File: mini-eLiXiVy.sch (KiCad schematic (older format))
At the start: 175 parts, among them J1 TYPE-C-31-M12_13_EDITED, J2 AVR-ISP-6, SW1 SW_Push, U1 ATmega32U4-AU, U2 WE-TVS-82400102, Y1 Crystal_GND24_Small

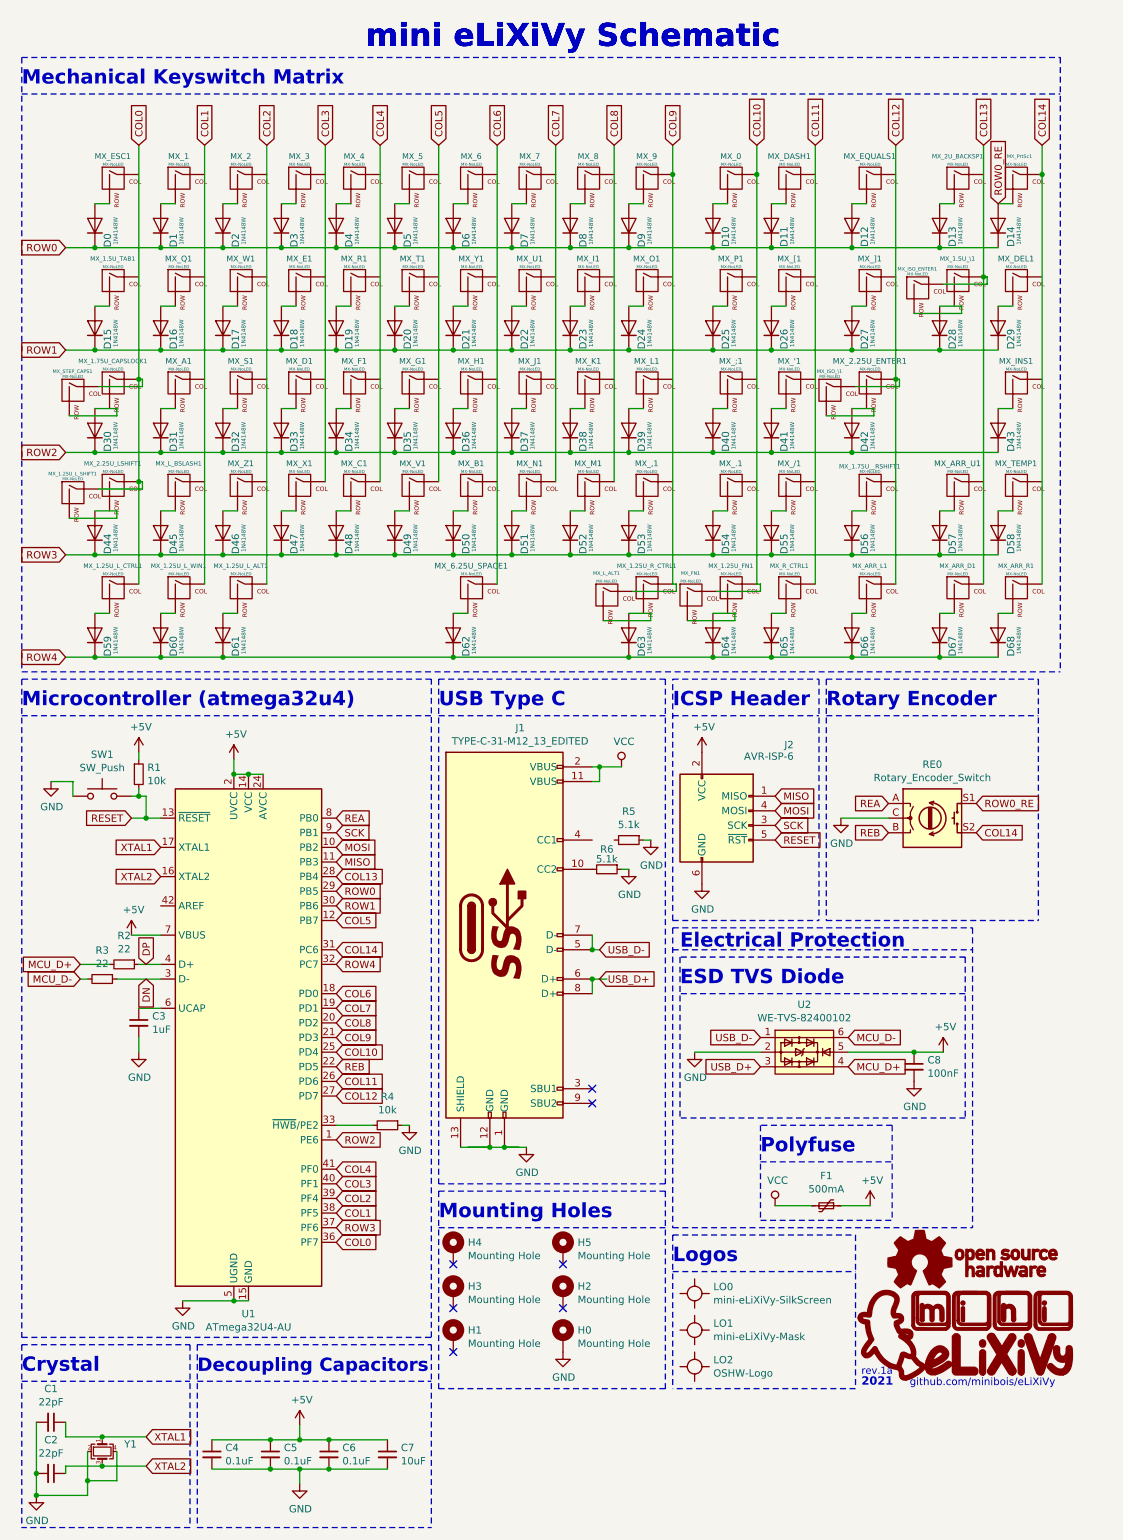
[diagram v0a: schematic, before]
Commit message: Reconnected some of the traces
After changing library locations around, some switches were disconnected in the schematic.
Had to reconnect those.
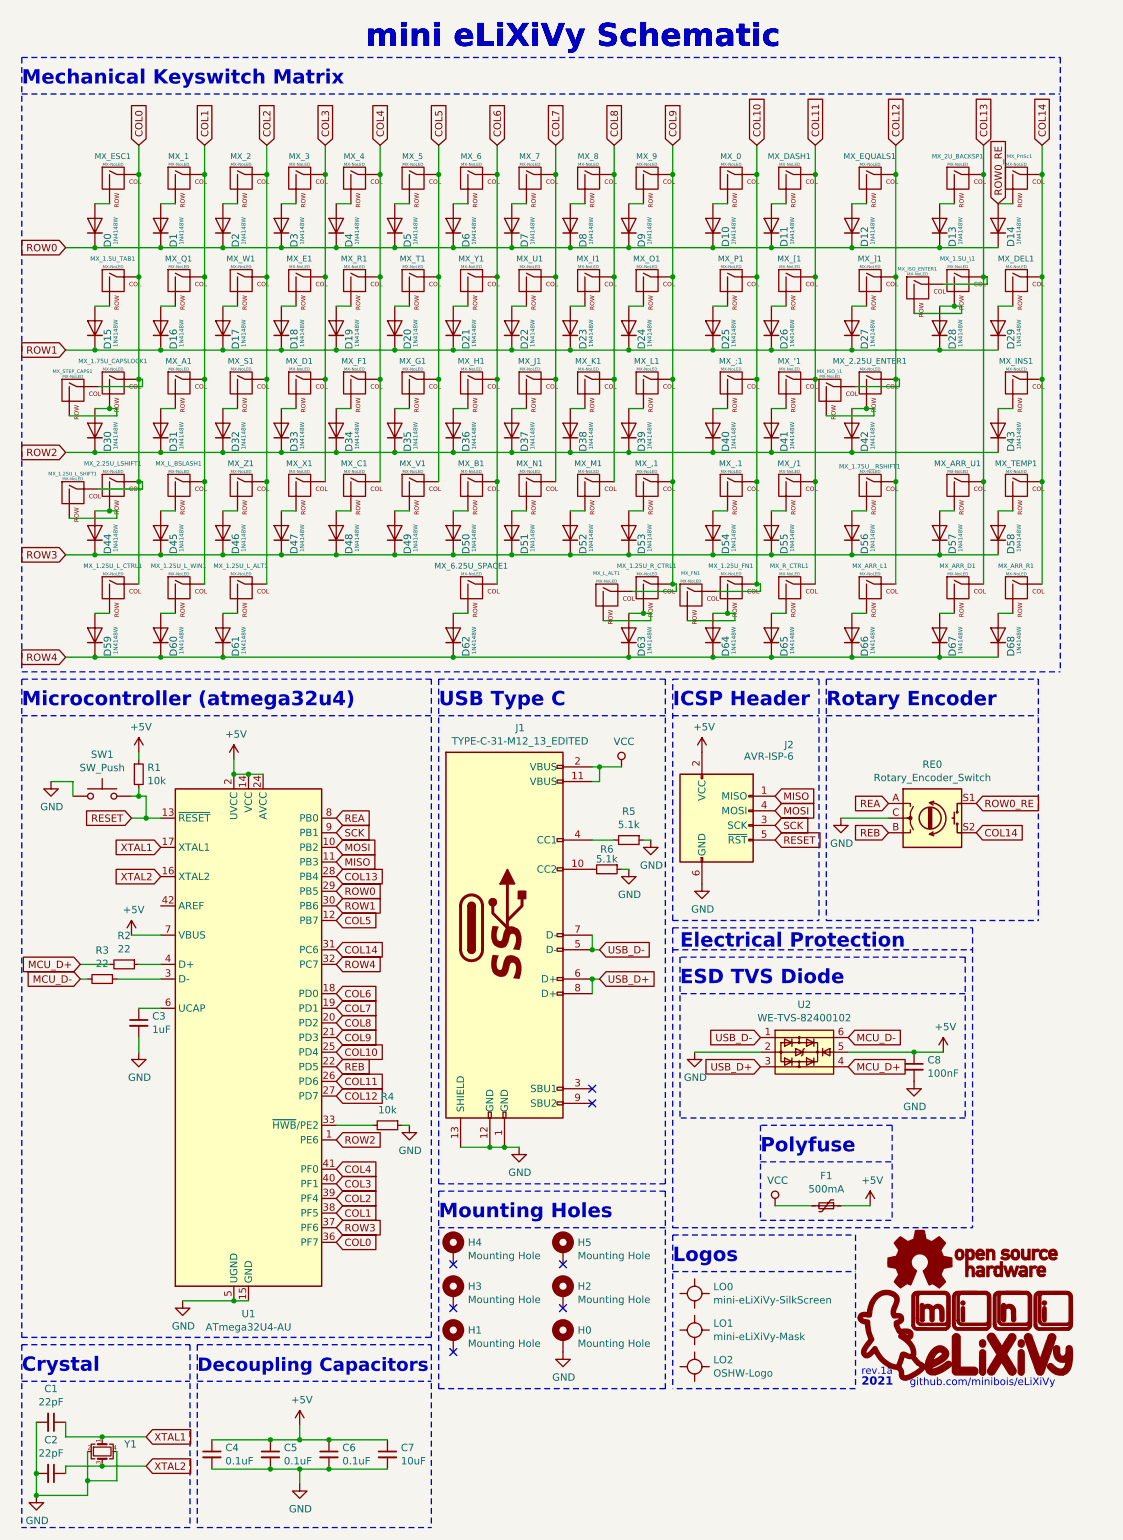
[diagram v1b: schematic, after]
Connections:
- net COL0: now also MX_1.5U_TAB1.1 (COL), MX_ESC1.1 (COL)
- net COL1: now also MX_1.1 (COL), MX_A1.1 (COL), MX_L_BSLASH1.1 (COL), MX_Q1.1 (COL)
- net COL10: now also MX_.1.1 (COL), MX_;1.1 (COL), MX_P1.1 (COL)
- net COL11: now also MX_'1.1 (COL), MX_/1.1 (COL), MX_DASH1.1 (COL), MX_[1.1 (COL)
- net COL12: now also MX_1.75U__RSHIFT1.1 (COL), MX_EQUALS1.1 (COL), MX_]1.1 (COL)
- net COL13: now also MX_2U_BACKSP1.1 (COL), MX_ARR_U1.1 (COL)
- net COL14: now also MX_DEL1.1 (COL), MX_INS1.1 (COL), MX_TEMP1.1 (COL)
- net COL2: now also MX_2.1 (COL), MX_S1.1 (COL), MX_W1.1 (COL), MX_Z1.1 (COL)
- net COL3: now also MX_3.1 (COL), MX_D1.1 (COL), MX_E1.1 (COL)
- net COL4: now also MX_4.1 (COL), MX_F1.1 (COL), MX_R1.1 (COL)
- net COL5: now also MX_5.1 (COL), MX_G1.1 (COL), MX_T1.1 (COL)
- net COL6: now also MX_6.1 (COL), MX_B1.1 (COL), MX_H1.1 (COL), MX_Y1.1 (COL)
- net COL7: now also MX_7.1 (COL), MX_J1.1 (COL), MX_U1.1 (COL)
- net COL8: now also MX_8.1 (COL), MX_I1.1 (COL), MX_K1.1 (COL)
- net COL9: now also MX_,1.1 (COL), MX_L1.1 (COL), MX_O1.1 (COL)
- net at MX_1.75U_CAPSLOCK1.2 (ROW): now also D30.2 (A), MX_STEP_CAPS1.2 (ROW)
- net at MX_2.25U_LSHIFT1.2 (ROW): now also D44.2 (A), MX_1.25U_L_SHIFT1.2 (ROW)
- net at MX_1.25U_R_CTRL1.2 (ROW): now also D63.2 (A), MX_L_ALT1.2 (ROW)
- net at MX_1.25U_FN1.2 (ROW): now also D64.2 (A), MX_FN1.2 (ROW)
- net at MX_2.25U_ENTER1.2 (ROW): now also D42.2 (A), MX_ISO_\1.2 (ROW)
- net at MX_1.5U_\1.2 (ROW): now also D28.2 (A), MX_ISO_ENTER1.2 (ROW)
- net at R5.2: now also J1.4 (CC1)
- net DN: no longer names the net of R3.1, U1.3 (D-)
- net DP: no longer names the net of R2.1, U1.4 (D+)
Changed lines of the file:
@@
 	6275 3500 7275 3500
 Wire Wire Line
-	6275 2800 6875 2800
-Wire Wire Line
 	6275 2100 6875 2100
-Wire Wire Line
-	6700 2550 7025 2550
 Wire Wire Line
 	6900 2350 7200 2350
@@
 Connection ~ 1550 3500
 Connection ~ 1975 3500
-Connection ~ 1100 3500
-Wire Wire Line
-	1100 3500 1550 3500
 Wire Wire Line
 	1550 4200 1975 4200
@@
 	1975 3500 2375 3500
 Wire Wire Line
-	900  3500 1100 3500
-Wire Wire Line
-	6875 2800 7275 2800
-Connection ~ 6875 2800
-Wire Wire Line
 	5325 2800 5725 2800
 Wire Wire Line
@@
 Wire Wire Line
 	900  2100 1100 2100
-Connection ~ 7175 2300
 Wire Wire Line
 	7200 2300 7200 2350
 Wire Wire Line
 	7175 2300 7200 2300
-Connection ~ 6575 3000
 Wire Wire Line
 	6600 3000 6600 3050
@@
 $EndComp
 $Comp
-L Diode:1N4148W D30
-U 1 1 622FC3F7
-P 1100 3350
-F 0 "D30" H 1095 3263 50  0000 R CNN
-F 1 "1N4148W" H 1159 3208 28  0000 R CNN
-F 2 "mini-general-tweaks:D_SOD123_axial-dual" H 1100 3175 50  0001 C CNN
-F 3 "https://www.vishay.com/docs/85748/1n4148w.pdf" H 1100 3350 50  0001 C CNN
-	1    1100 3350
-	0    -1   -1   0
-$EndComp
-$Comp
 L Diode:1N4148W D15
 U 1 1 622EF341
@@
 	1    0    0    -1
 $EndComp
-Wire Wire Line
-	7025 2500 7025 2550
 Wire Wire Line
 	5825 4600 5725 4600
@@
 Text Notes 2950 750  0    157  ~ 31
 mini eLiXiVy Schematic
-Connection ~ 5050 1600
-Wire Wire Line
-	5050 1600 5050 1400
-Connection ~ 5625 1600
 Wire Wire Line
 	5625 1600 5625 1400
-Connection ~ 7575 1600
 Wire Wire Line
 	7575 1600 7575 1400
@@
 Text Notes 3450 5250 0    98   ~ 20
 USB Type C
-Connection ~ 4500 7100
 Connection ~ 4500 6900
 Wire Wire Line
@@
 L power:GND #PWR0101
 U 1 1 607575CF
-P 4050 8250
-F 0 "#PWR0101" H 4050 8000 50  0001 C CNN
-F 1 "GND" H 4055 8077 50  0000 C CNN
-F 2 "" H 4050 8250 50  0001 C CNN
-F 3 "" H 4050 8250 50  0001 C CNN
-	1    4050 8250
-	1    0    0    -1
-$EndComp
-Wire Wire Line
-	3600 8250 3800 8250
-Connection ~ 3800 8250
-Wire Wire Line
-	3800 8250 3900 8250
-Connection ~ 3900 8250
-Wire Wire Line
-	3900 8250 4000 8250
+P 4000 8250
+F 0 "#PWR0101" H 4000 8000 50  0001 C CNN
+F 1 "GND" H 4005 8077 50  0000 C CNN
+F 2 "" H 4000 8250 50  0001 C CNN
+F 3 "" H 4000 8250 50  0001 C CNN
+	1    4000 8250
+	1    0    0    -1
+$EndComp
 $Comp
 L Device:R_Small R5
@@
 Text Notes 2950 750  0    157  ~ 31
 mini eLiXiVy Schematic
-Text GLabel 1450 7000 1    50   Input ~ 0
-DP
-Text GLabel 1450 7100 3    50   Input ~ 0
-DN
 Text Notes 6670 9892 0    51   ~ 0
 github.com/minibois/eLiXiVy
@@
 	5050 8800 7100 8800
 Wire Wire Line
-	7175 2300 7175 4400
-Wire Wire Line
-	7175 1400 7175 2300
-Wire Wire Line
-	6575 3000 6575 4400
-Wire Wire Line
-	6875 2500 7025 2500
-Wire Wire Line
-	4750 4600 4900 4600
-Wire Wire Line
-	6275 3200 6425 3200
-Wire Wire Line
-	1100 3200 1250 3200
-Wire Wire Line
-	1100 3900 1250 3900
-Wire Wire Line
-	5325 4600 5475 4600
-Wire Wire Line
-	3650 8250 3800 8250
-Wire Wire Line
-	5050 1600 5050 4400
-Wire Wire Line
-	5625 1600 5625 4400
-Wire Wire Line
-	7575 1600 7575 4400
-Wire Wire Line
-	3900 8250 4050 8250
-Wire Wire Line
-	1400 1400 1400 3000
-Wire Wire Line
-	1850 1400 1850 4400
-Wire Wire Line
-	2275 1400 2275 4400
-Wire Wire Line
-	2675 1400 2675 3700
-Wire Wire Line
-	3050 1400 3050 3700
-Wire Wire Line
-	3450 1400 3450 3700
-Wire Wire Line
-	3850 1400 3850 4400
-Wire Wire Line
-	4250 1400 4250 3700
-Wire Wire Line
-	4650 1400 4650 3700
-Wire Wire Line
-	6025 1400 6025 4400
-Wire Wire Line
-	6575 1400 6575 3000
-Wire Wire Line
-	4500 7100 4600 7100
+	6875 2500 6975 2500
 Wire Notes Line
 	7100 6750 7100 8800
@@
 Wire Wire Line
 	1400 5850 1450 5850
+Wire Wire Line
+	1100 3900 1200 3900
+Connection ~ 1200 3900
+Wire Wire Line
+	1200 3900 1250 3900
+Wire Wire Line
+	1850 4400 1850 3700
+Connection ~ 1850 1600
+Wire Wire Line
+	1850 1600 1850 1400
+Connection ~ 1850 2300
+Wire Wire Line
+	1850 2300 1850 1600
+Connection ~ 1850 3000
+Wire Wire Line
+	1850 3000 1850 2300
+Connection ~ 1850 3700
+Wire Wire Line
+	1850 3700 1850 3000
+Wire Wire Line
+	1400 1400 1400 1600
+Connection ~ 1400 1600
+Wire Wire Line
+	1400 1600 1400 2300
+Connection ~ 1400 2300
+Wire Wire Line
+	1400 2300 1400 3000
+Wire Wire Line
+	2275 1400 2275 1600
+Connection ~ 2275 1600
+Wire Wire Line
+	2275 1600 2275 2300
+Connection ~ 2275 2300
+Wire Wire Line
+	2275 2300 2275 3000
+Connection ~ 2275 3000
+Wire Wire Line
+	2275 3000 2275 3700
+Connection ~ 2275 3700
+Wire Wire Line
+	2275 3700 2275 4400
+Wire Wire Line
+	2675 1400 2675 1600
+Connection ~ 2675 1600
+Wire Wire Line
+	2675 1600 2675 2300
+Connection ~ 2675 2300
+Wire Wire Line
+	2675 2300 2675 3000
+Wire Wire Line
+	3050 1400 3050 1600
+Connection ~ 3050 1600
+Wire Wire Line
+	3050 1600 3050 2300
+Connection ~ 3050 2300
+Wire Wire Line
+	3050 2300 3050 3000
+Wire Wire Line
+	3450 1400 3450 1600
+Connection ~ 3450 1600
+Wire Wire Line
+	3450 1600 3450 2300
+Connection ~ 3450 2300
+Wire Wire Line
+	3450 2300 3450 3000
+Wire Wire Line
+	2675 3000 2675 3700
+Connection ~ 2675 3000
+Wire Wire Line
+	3050 3700 3050 3000
+Connection ~ 3050 3000
+Wire Wire Line
+	3450 3000 3450 3700
+Connection ~ 3450 3000
+Wire Wire Line
+	3850 3700 3850 3000
+Connection ~ 3850 1600
+Wire Wire Line
+	3850 1600 3850 1400
+Connection ~ 3850 2300
+Wire Wire Line
+	3850 2300 3850 1600
+Connection ~ 3850 3000
+Wire Wire Line
+	3850 3000 3850 2300
+Wire Wire Line
+	4250 1400 4250 1600
+Connection ~ 4250 1600
+Wire Wire Line
+	4250 1600 4250 2300
+Connection ~ 4250 2300
+Wire Wire Line
+	4250 2300 4250 3000
+Connection ~ 4250 3000
+Wire Wire Line
+	4250 3000 4250 3700
+Wire Wire Line
+	3850 4400 3850 3700
+Connection ~ 3850 3700
+Wire Wire Line
+	5050 4400 5050 3700
+Connection ~ 5050 4400
+Connection ~ 5050 1600
+Wire Wire Line
+	5050 1600 5050 1400
+Connection ~ 5050 2300
+Wire Wire Line
+	5050 2300 5050 1600
+Connection ~ 5050 3000
+Wire Wire Line
+	5050 3000 5050 2300
+Connection ~ 5050 3700
+Wire Wire Line
+	5050 3700 5050 3000
+Wire Wire Line
+	4650 1400 4650 1600
+Connection ~ 4650 1600
+Wire Wire Line
+	4650 1600 4650 2300
+Connection ~ 4650 2300
+Wire Wire Line
+	4650 2300 4650 3000
+Connection ~ 4650 3000
+Wire Wire Line
+	4650 3000 4650 3700
+Wire Wire Line
+	6025 4400 6025 3700
+Connection ~ 6025 1600
+Wire Wire Line
+	6025 1600 6025 1400
+Connection ~ 6025 2300
+Wire Wire Line
+	6025 2300 6025 1600
+Connection ~ 6025 3000
+Wire Wire Line
+	6025 3000 6025 2300
+Connection ~ 6025 3700
+Wire Wire Line
+	6025 3700 6025 3000
+Wire Wire Line
+	6575 1400 6575 1600
+Connection ~ 6575 1600
+Wire Wire Line
+	6575 1600 6575 2300
+Connection ~ 6575 2300
+Wire Wire Line
+	6575 2300 6575 3000
+Connection ~ 6575 3000
+Wire Wire Line
+	6575 3000 6575 3700
+Connection ~ 6575 3700
+Wire Wire Line
+	6575 3700 6575 4400
+Wire Wire Line
+	7175 4400 7175 3700
+Connection ~ 7175 1600
+Wire Wire Line
+	7175 1600 7175 1400
+Connection ~ 7175 2300
+Wire Wire Line
+	7175 2300 7175 1600
+Connection ~ 7175 3700
+Wire Wire Line
+	7175 3700 7175 2300
+Wire Wire Line
+	7575 1600 7575 2300
+Connection ~ 7575 1600
+Connection ~ 7575 2300
+Wire Wire Line
+	7575 2300 7575 3000
+Connection ~ 7575 3000
+Wire Wire Line
+	7575 3000 7575 3700
+Connection ~ 7575 3700
+Wire Wire Line
+	7575 3700 7575 4400
+Wire Wire Line
+	1100 3200 1200 3200
+Connection ~ 1200 3200
+Wire Wire Line
+	1200 3200 1250 3200
+Wire Wire Line
+	6275 2800 6875 2800
+Connection ~ 6875 2800
+Wire Wire Line
+	6875 2800 7275 2800
+Connection ~ 6975 2500
+Wire Wire Line
+	6975 2500 7025 2500
+Wire Wire Line
+	6700 2550 7025 2550
+Wire Wire Line
+	7025 2550 7025 2500
+Wire Wire Line
+	6275 3200 6375 3200
+Connection ~ 6375 3200
+Wire Wire Line
+	6375 3200 6425 3200
+Wire Wire Line
+	5625 4400 5625 3700
+Connection ~ 5625 4400
+Connection ~ 5625 1600
+Connection ~ 5625 2300
+Wire Wire Line
+	5625 2300 5625 1600
+Connection ~ 5625 3000
+Wire Wire Line
+	5625 3000 5625 2300
+Connection ~ 5625 3700
+Wire Wire Line
+	5625 3700 5625 3000
+Wire Wire Line
+	1100 3500 1550 3500
+Connection ~ 1100 3500
+Wire Wire Line
+	900  3500 1100 3500
+$Comp
+L Diode:1N4148W D30
+U 1 1 622FC3F7
+P 1100 3350
+F 0 "D30" H 1095 3263 50  0000 R CNN
+F 1 "1N4148W" H 1159 3208 28  0000 R CNN
+F 2 "mini-general-tweaks:D_SOD123_axial-dual" H 1100 3175 50  0001 C CNN
+F 3 "https://www.vishay.com/docs/85748/1n4148w.pdf" H 1100 3350 50  0001 C CNN
+	1    1100 3350
+	0    -1   -1   0
+$EndComp
+Wire Wire Line
+	4500 7100 4550 7100
+Connection ~ 4500 7100
+Wire Wire Line
+	4500 6150 4650 6150
+Wire Wire Line
+	3600 8250 3800 8250
+Connection ~ 3800 8250
+Wire Wire Line
+	3800 8250 3900 8250
+Connection ~ 3900 8250
+Wire Wire Line
+	3900 8250 4000 8250
+Wire Wire Line
+	4750 4600 4850 4600
+Connection ~ 4850 4600
+Wire Wire Line
+	4850 4600 4900 4600
+Wire Wire Line
+	5325 4600 5425 4600
+Connection ~ 5425 4600
+Wire Wire Line
+	5425 4600 5475 4600
 $EndSCHEMATC
